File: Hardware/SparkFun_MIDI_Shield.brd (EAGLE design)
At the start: 59.7 x 53.3 mm, 36 parts, among them J1 MIDI IN, J2 MIDI OUT, J3 UNO_R3_SHIELD, U1 6N138M, U2 74AHC1G125

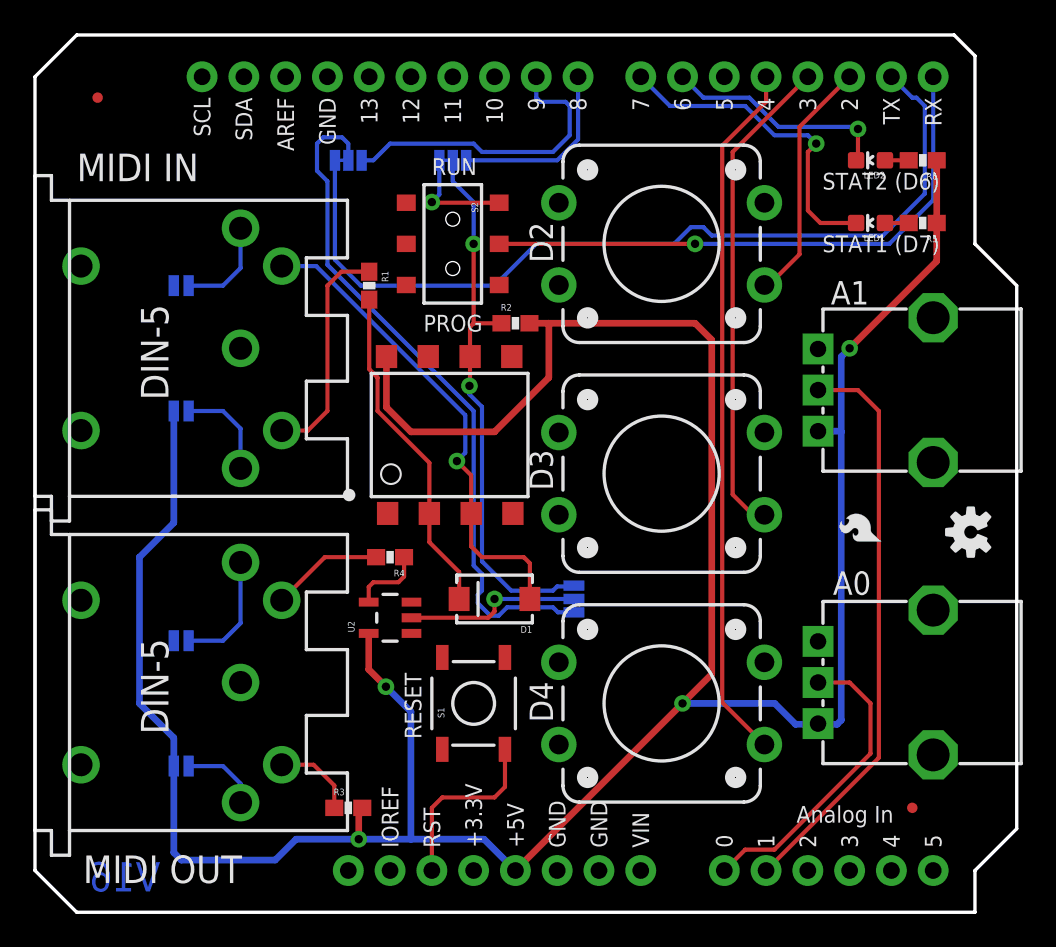
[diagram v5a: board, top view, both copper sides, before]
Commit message: Updates based on QC checklist.
-Measures layer populated.
-U1 got name/value.
-Added stubs to some parts on schem.
-Version # back to 1.5.
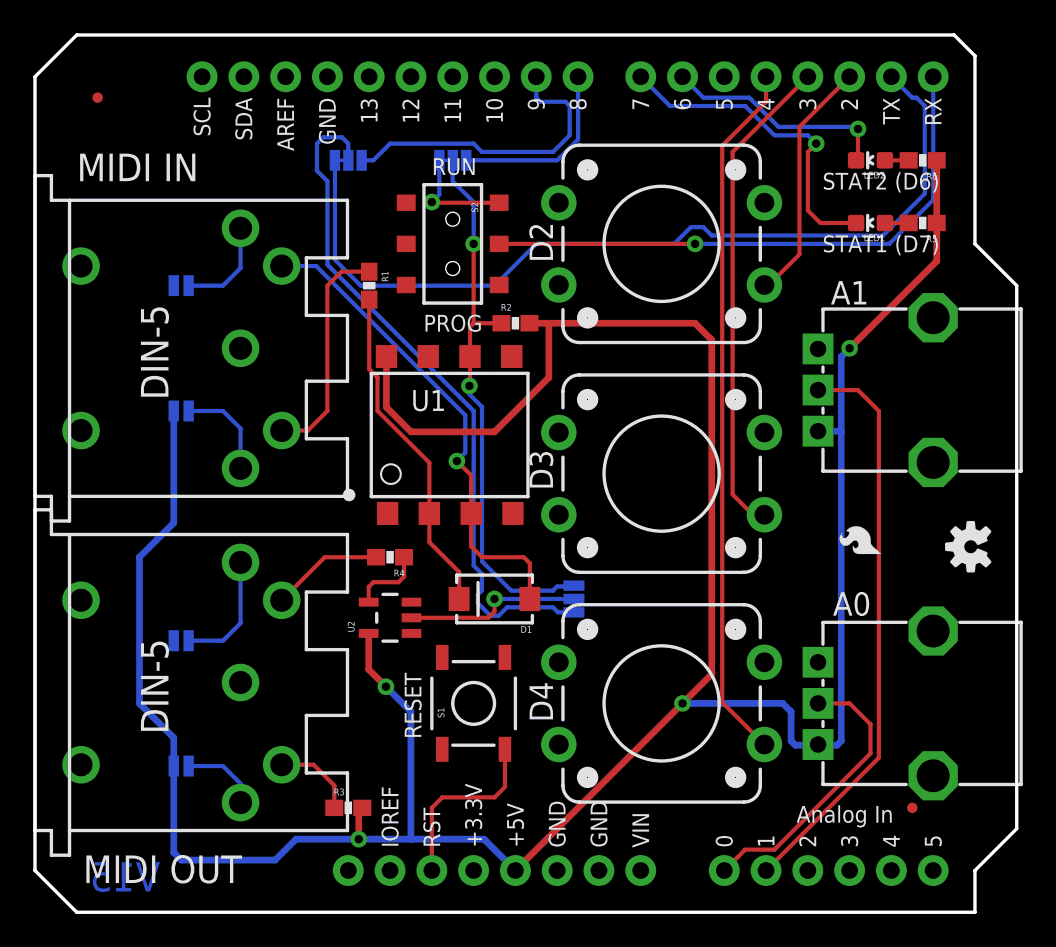
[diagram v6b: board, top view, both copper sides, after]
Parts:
- moved RV2 1.27 mm to (54.6, 12.7)
- moved LOGO2 0.89 mm to (56.9, 22.2)
- moved LOGO5 0.76 mm to (51.8, 21.5)
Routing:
- net VCC: track 181.7 -> 184.5 mm
- net A0: track 18.6 -> 17.3 mm
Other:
- board text added: "5-pin DIN connectors need approx 0.53" (13.5mm) diam holes"
- board text added: "All units in Inches"
- board text added: "Pot shafts are 0.24" (6mm) diameter"
- board text added: "V15"
- board text removed: "V16"
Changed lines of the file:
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@@
 <setting verticaltext="up"/>
 </settings>
-<grid distance="0.01" unitdist="inch" unit="inch" style="lines" multiple="1" display="yes" altdistance="0.001" altunitdist="inch" altunit="inch"/>
+<grid distance="0.05" unitdist="inch" unit="inch" style="lines" multiple="1" display="yes" altdistance="0.005" altunitdist="inch" altunit="inch"/>
 <layers>
 <layer number="1" name="Top" color="4" fill="1" visible="yes" active="yes"/>
@@
 <layer number="43" name="vRestrict" color="2" fill="10" visible="no" active="yes"/>
 <layer number="44" name="Drills" color="7" fill="1" visible="no" active="yes"/>
-<layer number="45" name="Holes" color="7" fill="1" visible="no" active="yes"/>
+<layer number="45" name="Holes" color="7" fill="1" visible="yes" active="yes"/>
 <layer number="46" name="Milling" color="3" fill="1" visible="no" active="yes"/>
 <layer number="47" name="Measures" color="7" fill="1" visible="no" active="yes"/>
@@
 <layer number="49" name="Reference" color="7" fill="1" visible="no" active="yes"/>
 <layer number="50" name="dxf" color="7" fill="1" visible="no" active="yes"/>
-<layer number="51" name="tDocu" color="6" fill="1" visible="no" active="yes"/>
+<layer number="51" name="tDocu" color="6" fill="1" visible="yes" active="yes"/>
 <layer number="52" name="bDocu" color="7" fill="1" visible="no" active="yes"/>
 <layer number="53" name="tGND_GNDA" color="7" fill="9" visible="no" active="no"/>
@@
 <text x="31.496" y="11.557" size="1.4224" layer="21" font="vector" ratio="15" rot="R90">D4</text>
 <text x="48.387" y="36.957" size="1.4224" layer="21" font="vector" ratio="15">A1</text>
-<text x="48.514" y="19.304" size="1.4224" layer="21" font="vector" ratio="15">A0</text>
+<text x="48.514" y="18.034" size="1.4224" layer="21" font="vector" ratio="15">A0</text>
 <text x="2.54" y="44.45" size="1.6764" layer="21" font="vector" ratio="15">MIDI IN</text>
 <text x="2.921" y="1.778" size="1.6764" layer="21" font="vector" ratio="15">MIDI OUT</text>
@@
 <text x="7.62" y="19.05" size="1.016" layer="22" font="vector" ratio="15" rot="MR180">SJ6</text>
 <text x="7.62" y="7.62" size="1.016" layer="22" font="vector" ratio="15" rot="MR180">SJ7</text>
-<text x="7.62" y="1.27" size="1.778" layer="16" font="vector" ratio="15" rot="MR0">V16</text>
+<text x="7.62" y="1.27" size="1.778" layer="16" font="vector" ratio="15" rot="MR0">V15</text>
 <text x="23.876" y="48.006" size="1.016" layer="22" font="vector" ratio="15" rot="MR180">SJ1</text>
 <text x="17.526" y="48.006" size="1.016" layer="22" font="vector" ratio="15" rot="MR180">SJ2</text>
@@
 <text x="34.036" y="22.098" size="1.016" layer="22" font="vector" ratio="15" rot="SMR270" align="top-left">SJ3 selects out type</text>
 <text x="17.78" y="-14.224" size="1.778" layer="51" font="vector" ratio="12">Chris Taylor</text>
+<dimension x1="2.54" y1="0" x2="2.54" y2="53.34" x3="-13.97" y3="26.67" textsize="1.27" textratio="15" layer="47" dtype="vertical" unit="inch"/>
+<dimension x1="2.54" y1="0" x2="0" y2="13.97" x3="-2.54" y3="6.985" textsize="1.27" textratio="15" layer="47" dtype="vertical" unit="inch"/>
+<dimension x1="2.54" y1="0" x2="0" y2="34.29" x3="-7.62" y3="17.145" textsize="1.27" textratio="15" layer="47" dtype="vertical" unit="inch"/>
+<text x="2.54" y="-21.59" size="1.778" layer="47" font="vector" ratio="15">All units in Inches</text>
+<dimension x1="59.69" y1="38.1" x2="0" y2="50.8" x3="29.845" y3="72.39" textsize="1.27" textratio="15" layer="47" dtype="horizontal" unit="inch"/>
+<dimension x1="38.1" y1="12.7" x2="0" y2="40.64" x3="19.05" y3="57.15" textsize="1.27" textratio="15" layer="47" dtype="horizontal" unit="inch"/>
+<dimension x1="54.61" y1="13.97" x2="0" y2="62.23" x3="27.305" y3="62.23" textsize="1.27" textratio="15" layer="47" dtype="horizontal" unit="inch"/>
+<dimension x1="57.15" y1="0" x2="54.61" y2="31.75" x3="73.66" y3="15.875" textsize="1.27" textratio="15" layer="47" dtype="vertical" unit="inch"/>
+<dimension x1="54.61" y1="31.75" x2="68.58" y2="44.45" x3="78.74" y3="44.45" textsize="1.778" textratio="15" layer="47" dtype="leader" unit="inch"/>
+<text x="77.47" y="45.72" size="1.27" layer="47" font="vector" ratio="15">Pot shafts are 0.24" (6mm) diameter</text>
+<dimension x1="0" y1="34.29" x2="-21.59" y2="44.45" x3="-33.02" y3="44.45" textsize="1.27" textratio="15" layer="47" dtype="leader" unit="inch"/>
+<text x="-53.34" y="45.72" size="1.27" layer="47" font="vector" ratio="15">5-pin DIN connectors need approx
+0.53" (13.5mm) diam holes</text>
+<dimension x1="38.1" y1="12.7" x2="38.1" y2="0" x3="63.5" y3="6.35" textsize="1.27" textratio="15" layer="47" dtype="vertical" unit="inch"/>
+<dimension x1="38.1" y1="26.67" x2="38.1" y2="0" x3="68.58" y3="13.335" textsize="1.27" textratio="15" layer="47" dtype="vertical" unit="inch"/>
+<dimension x1="38.1" y1="40.64" x2="38.1" y2="0" x3="78.74" y3="20.32" textsize="1.27" textratio="15" layer="47" dtype="vertical" unit="inch"/>
 </plain>
 <attributes>
@@
 <attribute name="PROD_ID" value="RES-09177" x="54.61" y="31.75" size="1.778" layer="27" rot="R180" display="off"/>
 </element>
-<element name="RV2" library="SparkFun-Electromechanical" package="ALPS_POT" value="10k" x="54.61" y="13.97" rot="R180">
-<attribute name="PROD_ID" value="RES-09177" x="54.61" y="13.97" size="1.778" layer="27" rot="R180" display="off"/>
+<element name="RV2" library="SparkFun-Electromechanical" package="ALPS_POT" value="10k" x="54.61" y="12.7" rot="R180">
+<attribute name="PROD_ID" value="RES-09177" x="54.61" y="12.7" size="1.778" layer="27" rot="R180" display="off"/>
 </element>
 <element name="J3" library="SparkFun-Boards" package="UNO_R3_SHIELD" value="UNO_R3_SHIELD" x="0" y="53.34" rot="R270"/>
@@
 <element name="SJ5" library="SparkFun-Passives" package="PAD-JUMPER-2-NO_YES_SILK" value="JUMPER-PAD-2-NOYES_SILK" x="8.89" y="30.48" rot="MR180"/>
 <element name="LOGO1" library="SparkFun-Aesthetics" package="SFE_LOGO_NAME_FLAME_.2" value="SFE_LOGO_NAME_FLAME.2_INCH" x="23.749" y="39.243" rot="MR270"/>
-<element name="LOGO2" library="SparkFun-Aesthetics" package="OSHW-LOGO-S" value="OSHW-LOGOS" x="56.896" y="23.114" rot="R90"/>
+<element name="LOGO2" library="SparkFun-Aesthetics" package="OSHW-LOGO-S" value="OSHW-LOGOS" x="56.896" y="22.225" rot="R90"/>
 <element name="LOGO3" library="SparkFun-Aesthetics" package="OSHW-LOGO-M" value="OSHW-LOGOM" x="38.1" y="26.67" rot="MR270"/>
-<element name="LOGO5" library="SparkFun-Aesthetics" package="SFE_LOGO_FLAME_.1" value="SFE_LOGO_FLAME.1_INCH" x="51.816" y="22.225" rot="R90"/>
+<element name="LOGO5" library="SparkFun-Aesthetics" package="SFE_LOGO_FLAME_.1" value="SFE_LOGO_FLAME.1_INCH" x="51.816" y="21.463" rot="R90"/>
 <element name="SJ1" library="SparkFun-Passives" package="PAD-JUMPER-3-2OF3_NC_BY_TRACE_YES_SILK_FULL_BOX" value="TX sel" x="25.4" y="45.72" rot="MR0"/>
 <element name="SJ2" library="SparkFun-Passives" package="PAD-JUMPER-3-2OF3_NC_BY_TRACE_YES_SILK_FULL_BOX" value="RX sel" x="19.05" y="45.72" rot="MR0"/>
@@
 <wire x1="49.53" y1="34.29" x2="49.022" y2="33.782" width="0.4064" layer="16"/>
 <wire x1="49.022" y1="33.782" x2="49.022" y2="29.21" width="0.4064" layer="16"/>
-<wire x1="49.022" y1="29.21" x2="49.022" y2="11.684" width="0.4064" layer="16"/>
+<wire x1="49.022" y1="29.21" x2="49.022" y2="10.414" width="0.4064" layer="16"/>
 <wire x1="54.825" y1="39.585" x2="49.53" y2="34.29" width="0.4064" layer="1"/>
 <via x="49.53" y="34.29" extent="1-16" drill="0.508"/>
-<wire x1="48.768" y1="11.43" x2="49.022" y2="11.684" width="0.4064" layer="16"/>
-<wire x1="44.974" y1="12.7" x2="39.37" y2="12.7" width="0.4064" layer="16"/>
-<wire x1="46.244" y1="11.43" x2="44.974" y2="12.7" width="0.4064" layer="16"/>
+<wire x1="48.768" y1="10.16" x2="49.022" y2="10.414" width="0.4064" layer="16"/>
+<wire x1="45.466" y1="12.7" x2="39.37" y2="12.7" width="0.4064" layer="16"/>
 <via x="39.37" y="12.7" extent="1-16" drill="0.508"/>
-<wire x1="47.61" y1="11.47" x2="47.57" y2="11.43" width="0.4064" layer="16"/>
-<wire x1="47.57" y1="11.43" x2="46.244" y2="11.43" width="0.4064" layer="16"/>
-<wire x1="47.61" y1="11.47" x2="47.65" y2="11.43" width="0.4064" layer="16"/>
-<wire x1="47.65" y1="11.43" x2="48.768" y2="11.43" width="0.4064" layer="16"/>
+<wire x1="47.61" y1="10.2" x2="47.57" y2="10.16" width="0.4064" layer="16"/>
+<wire x1="47.57" y1="10.16" x2="46.228" y2="10.16" width="0.4064" layer="16"/>
+<wire x1="47.61" y1="10.2" x2="47.65" y2="10.16" width="0.4064" layer="16"/>
+<wire x1="47.65" y1="10.16" x2="48.768" y2="10.16" width="0.4064" layer="16"/>
 <wire x1="47.61" y1="29.25" x2="48.982" y2="29.25" width="0.4064" layer="16"/>
 <wire x1="48.982" y1="29.25" x2="49.022" y2="29.21" width="0.4064" layer="16"/>
 <wire x1="31.242" y1="32.512" x2="31.242" y2="35.814" width="0.4064" layer="1"/>
 <wire x1="27.94" y1="29.21" x2="31.242" y2="32.512" width="0.4064" layer="1"/>
+<wire x1="46.228" y1="10.16" x2="45.974" y2="10.414" width="0.4064" layer="16"/>
+<wire x1="45.974" y1="10.414" x2="45.974" y2="12.192" width="0.4064" layer="16"/>
+<wire x1="45.974" y1="12.192" x2="45.466" y2="12.7" width="0.4064" layer="16"/>
 </signal>
 <signal name="56">
@@
 <wire x1="43.18" y1="3.81" x2="44.958" y2="3.81" width="0.254" layer="1"/>
 <wire x1="44.958" y1="3.81" x2="50.8" y2="9.652" width="0.254" layer="1"/>
-<wire x1="50.8" y1="9.652" x2="50.8" y2="12.7" width="0.254" layer="1"/>
-<wire x1="50.8" y1="12.7" x2="49.53" y2="13.97" width="0.254" layer="1"/>
+<wire x1="50.8" y1="9.652" x2="50.8" y2="11.43" width="0.254" layer="1"/>
+<wire x1="50.8" y1="11.43" x2="49.53" y2="12.7" width="0.254" layer="1"/>
 <contactref element="RV2" pad="P$2"/>
-<wire x1="47.61" y1="13.97" x2="49.53" y2="13.97" width="0.254" layer="1"/>
+<wire x1="47.61" y1="12.7" x2="49.53" y2="12.7" width="0.254" layer="1"/>
 </signal>
 <signal name="N$9">

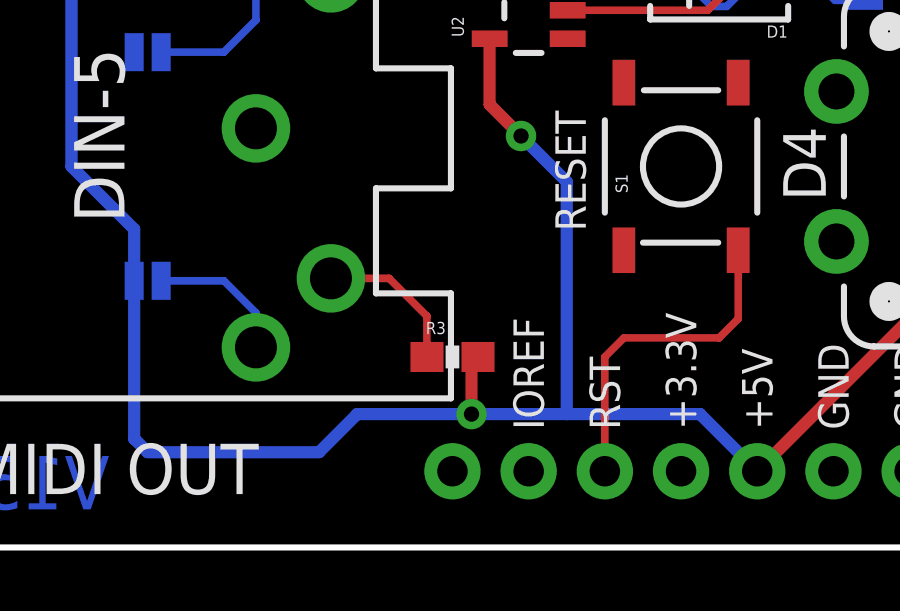
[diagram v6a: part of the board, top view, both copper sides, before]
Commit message: Fixing resistor obscured by output connector.
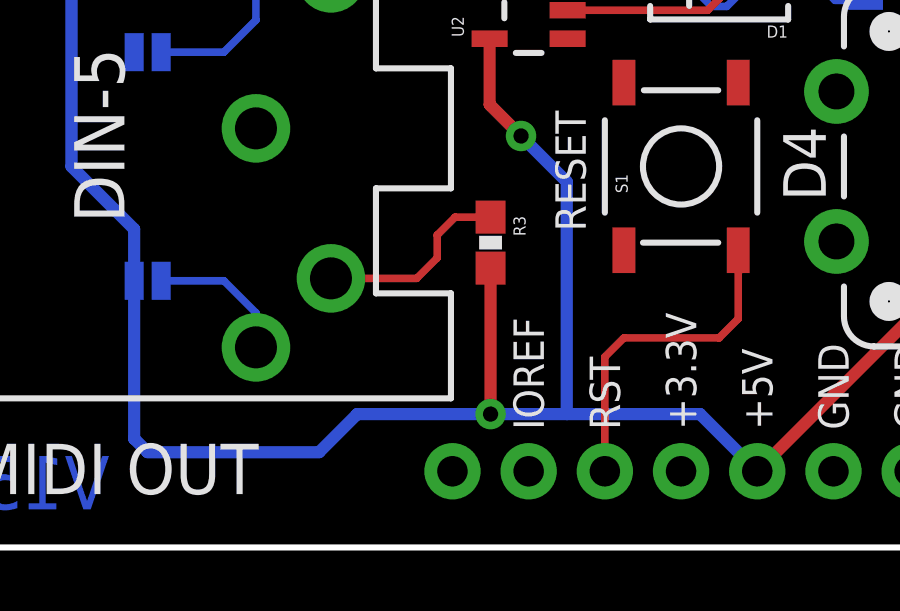
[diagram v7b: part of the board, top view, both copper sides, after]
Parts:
- moved R3 4.02 mm to (20.3, 10.2), turned to 270 degrees
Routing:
- net VCC: track 184.5 -> 187.3 mm
- net 1235: track 5.08 -> 6.61 mm
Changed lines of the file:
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@@
 <?xml version="1.0" encoding="utf-8"?>
 <!DOCTYPE eagle SYSTEM "eagle.dtd">
-<eagle version="7.1.0">
+<eagle version="7.3.0">
 <drawing>
 <settings>
@@
 <setting verticaltext="up"/>
 </settings>
-<grid distance="0.05" unitdist="inch" unit="inch" style="lines" multiple="1" display="yes" altdistance="0.005" altunitdist="inch" altunit="inch"/>
+<grid distance="0.01" unitdist="inch" unit="inch" style="lines" multiple="1" display="yes" altdistance="0.001" altunitdist="inch" altunit="inch"/>
 <layers>
 <layer number="1" name="Top" color="4" fill="1" visible="yes" active="yes"/>
@@
 <attribute name="VALUE" value="220" x="29.21" y="35.814" size="1.778" layer="27" display="off"/>
 </element>
-<element name="R3" library="SparkFun-Resistors" package="0603-RES" value="220" x="19.05" y="6.35">
-<attribute name="PROD_ID" value="RES-07861" x="19.05" y="6.35" size="1.778" layer="27" display="off"/>
-<attribute name="VALUE" value="220" x="19.05" y="6.35" size="1.778" layer="27" display="off"/>
+<element name="R3" library="SparkFun-Resistors" package="0603-RES" value="220" x="20.32" y="10.16" rot="R270">
+<attribute name="PROD_ID" value="RES-07861" x="20.32" y="10.16" size="1.778" layer="27" rot="R270" display="off"/>
+<attribute name="VALUE" value="220" x="20.32" y="10.16" size="1.778" layer="27" rot="R270" display="off"/>
 </element>
 <element name="R4" library="SparkFun-Resistors" package="0603-RES" value="220" x="21.59" y="21.59" rot="R180">
@@
 <contactref element="R5" pad="1"/>
 <contactref element="R2" pad="2"/>
-<via x="19.685" y="4.445" extent="1-16" drill="0.508"/>
-<wire x1="19.685" y1="4.445" x2="22.86" y2="4.445" width="0.4064" layer="16"/>
+<via x="20.32" y="4.445" extent="1-16" drill="0.508"/>
+<wire x1="20.32" y1="4.445" x2="22.86" y2="4.445" width="0.4064" layer="16"/>
 <wire x1="22.86" y1="4.445" x2="27.305" y2="4.445" width="0.4064" layer="16"/>
 <wire x1="54.825" y1="41.91" x2="54.825" y2="39.585" width="0.4064" layer="1"/>
 <wire x1="54.825" y1="45.72" x2="54.825" y2="41.91" width="0.4064" layer="1"/>
 <contactref element="U2" pad="5"/>
-<wire x1="19.685" y1="4.445" x2="19.685" y2="6.35" width="0.4064" layer="1"/>
 <contactref element="J3" pad="5V"/>
 <wire x1="29.21" y1="2.54" x2="27.305" y2="4.445" width="0.4064" layer="16"/>
@@
 <wire x1="21.37" y1="30.7" x2="22.86" y2="29.21" width="0.4064" layer="1"/>
 <wire x1="22.86" y1="29.21" x2="27.94" y2="29.21" width="0.4064" layer="1"/>
-<wire x1="19.9" y1="6.35" x2="19.685" y2="6.35" width="0.254" layer="1"/>
 <contactref element="SJ7" pad="1"/>
 <contactref element="SJ5" pad="1"/>
@@
 <wire x1="8.89" y1="3.175" x2="14.605" y2="3.175" width="0.4064" layer="16"/>
 <wire x1="14.605" y1="3.175" x2="15.875" y2="4.445" width="0.4064" layer="16"/>
-<wire x1="15.875" y1="4.445" x2="19.685" y2="4.445" width="0.4064" layer="16"/>
+<wire x1="15.875" y1="4.445" x2="20.32" y2="4.445" width="0.4064" layer="16"/>
 <wire x1="8.44" y1="30.48" x2="8.44" y2="23.68" width="0.4064" layer="16"/>
 <wire x1="8.44" y1="23.68" x2="6.35" y2="21.59" width="0.4064" layer="16"/>
@@
 <wire x1="45.974" y1="10.414" x2="45.974" y2="12.192" width="0.4064" layer="16"/>
 <wire x1="45.974" y1="12.192" x2="45.466" y2="12.7" width="0.4064" layer="16"/>
+<wire x1="20.32" y1="9.31" x2="20.32" y2="4.445" width="0.4064" layer="1"/>
 </signal>
 <signal name="56">
@@
 <contactref element="R3" pad="1"/>
 <contactref element="J2" pad="4"/>
-<wire x1="18.2" y1="6.35" x2="18.2" y2="7.708" width="0.254" layer="1"/>
-<wire x1="15" y1="8.97" x2="16.938" y2="8.97" width="0.254" layer="1"/>
-<wire x1="16.938" y1="8.97" x2="18.2" y2="7.708" width="0.254" layer="1"/>
+<wire x1="15" y1="8.97" x2="17.86" y2="8.97" width="0.254" layer="1"/>
+<wire x1="20.32" y1="11.01" x2="19.138" y2="11.01" width="0.254" layer="1"/>
+<wire x1="19.138" y1="11.01" x2="18.542" y2="10.414" width="0.254" layer="1"/>
+<wire x1="18.542" y1="10.414" x2="18.542" y2="9.652" width="0.254" layer="1"/>
+<wire x1="18.542" y1="9.652" x2="17.86" y2="8.97" width="0.254" layer="1"/>
 </signal>
 <signal name="D2">
